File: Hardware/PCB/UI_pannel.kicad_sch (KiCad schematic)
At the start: 0 parts

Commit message: added UI
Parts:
- added C? (x4): C, symbol Device:C
- added J2: FH34SRJ-24S-0.5SH(50), symbol FPC_Connectors:FH34SRJ-24S-0.5SH(50)
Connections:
- new net +18V: C?.1, C?.1, J2.21
- new net +3.3V: C?.1, C?.1, J2.22, J2.23
- new net GND: C?.2, C?.2, C?.2, C?.2, J2.1, J2.11, J2.14, J2.17, J2.18, J2.2, J2.20, J2.24, J2.5, J2.8
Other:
- note added: "Connector for screen"
- note added: "Screen"
- note added: "pwm for constan current"

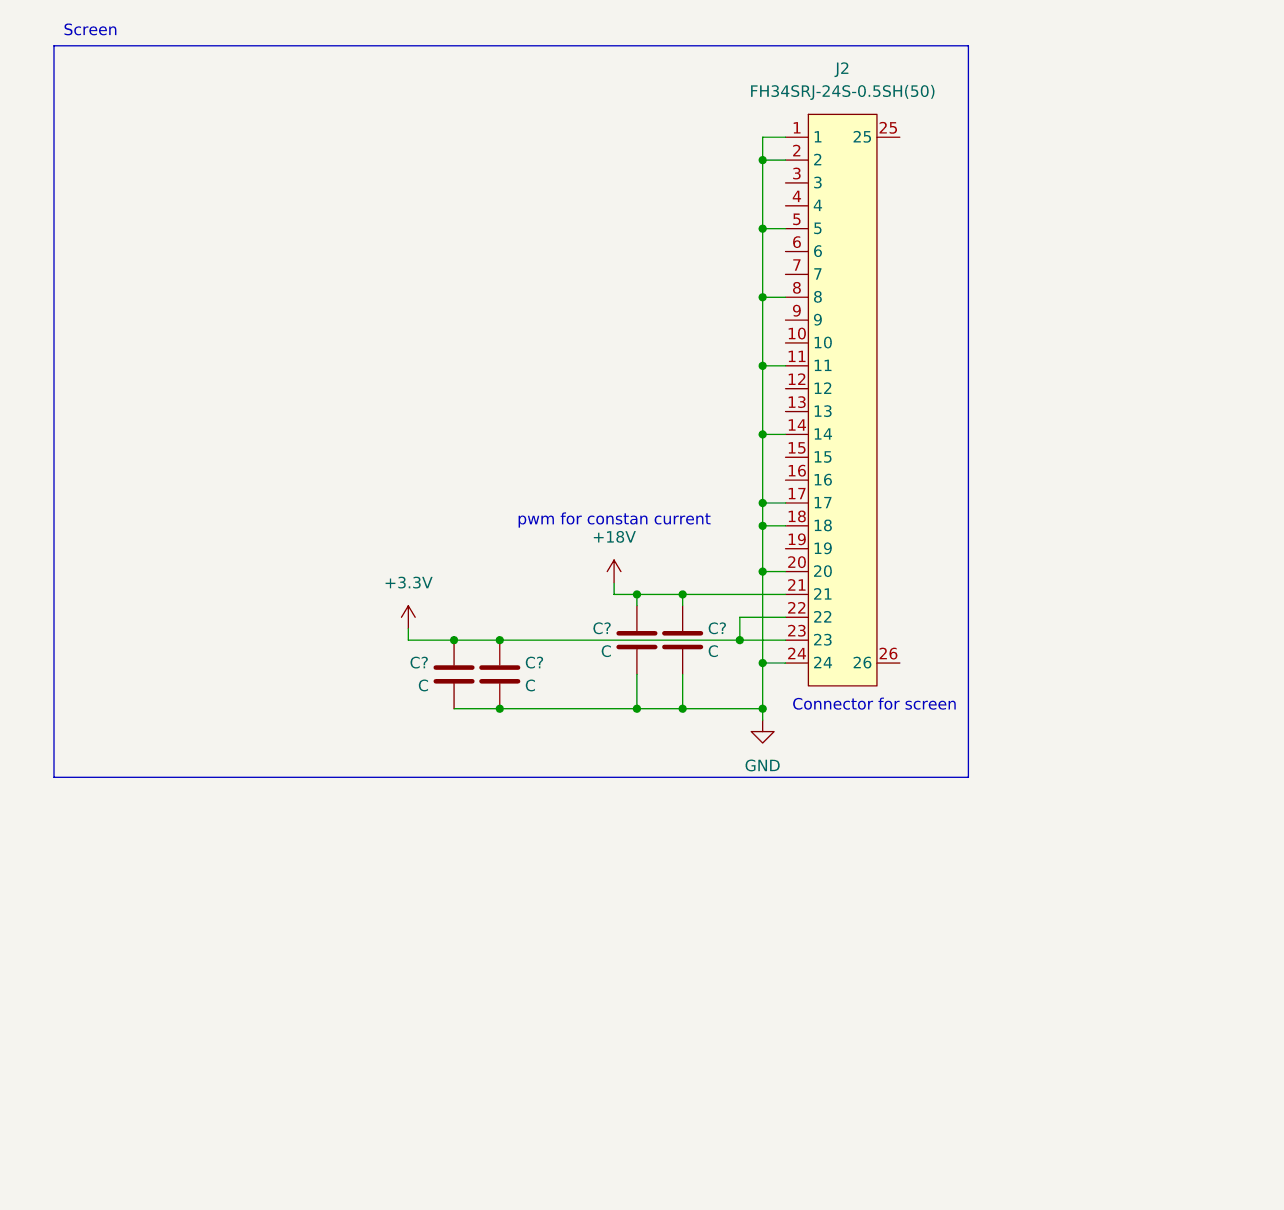
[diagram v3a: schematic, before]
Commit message: added buttons
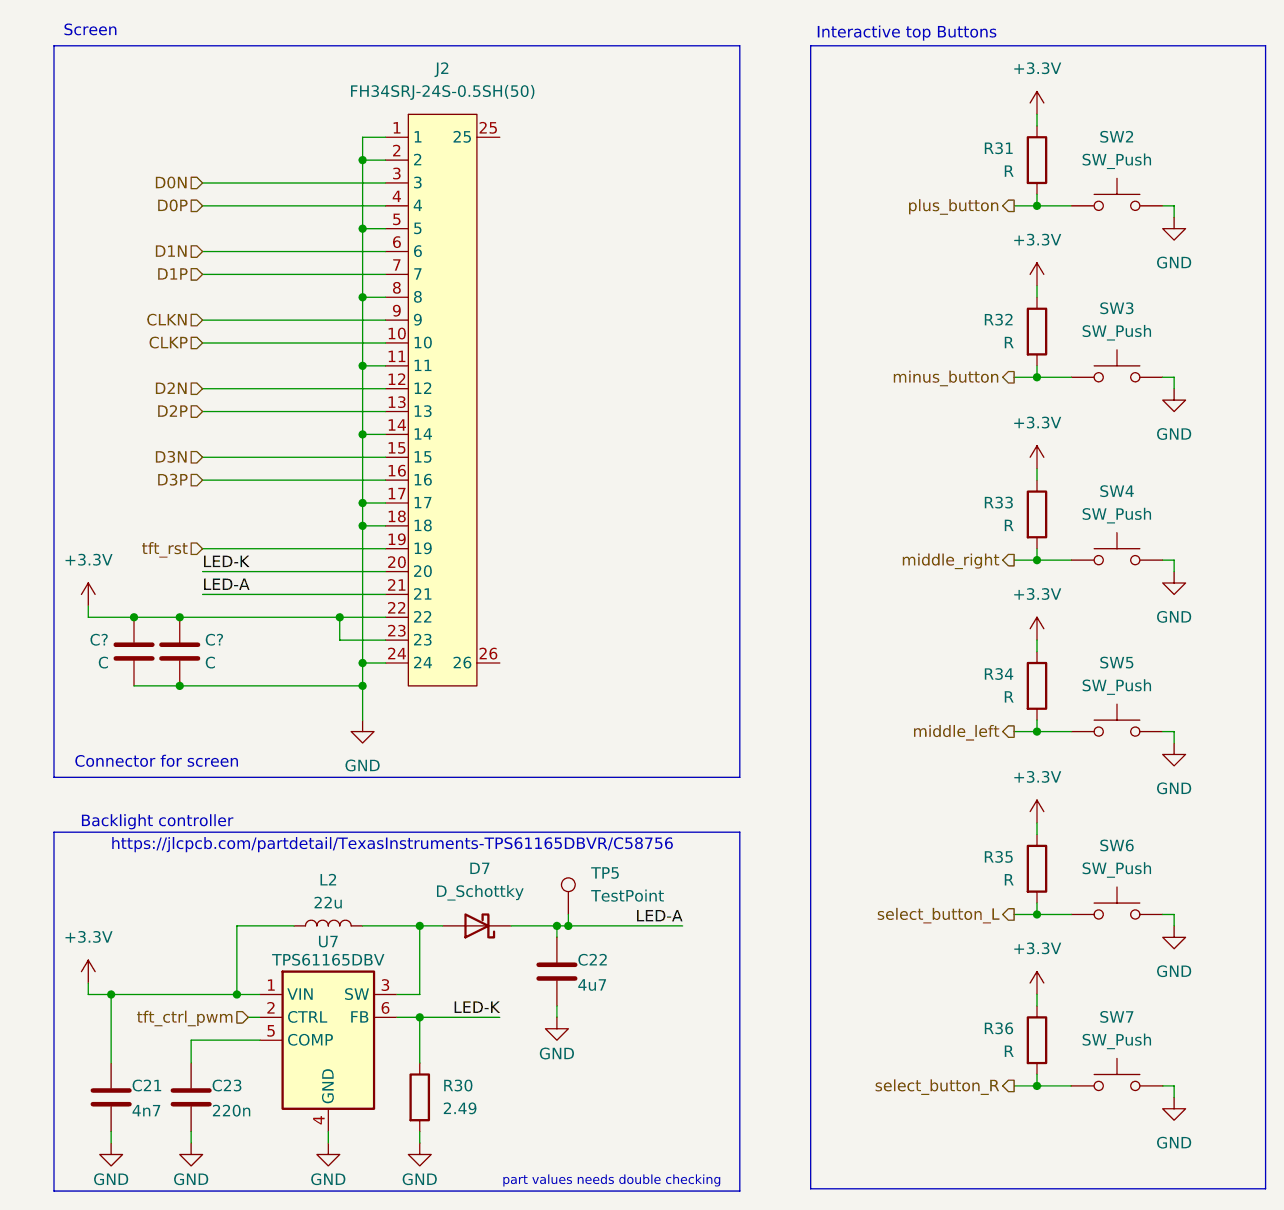
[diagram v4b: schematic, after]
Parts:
- removed C? (x2): C, symbol Device:C
- added C21: 4n7, symbol Device:C
- added C22: 4u7, symbol Device:C
- added C23: 220n, symbol Device:C
- added D7: D_Schottky, symbol Device:D_Schottky
- added L2: 22u, symbol Device:L
- added R30: 2.49, symbol Device:R
- added R31, R32, R33, R34, R35, R36: R, symbol Device:R
- added SW2, SW3, SW4, SW5, SW6, SW7: SW_Push, symbol Switch:SW_Push
- added TP5: TestPoint, symbol Connector:TestPoint
- added U7: TPS61165DBV, Package_TO_SOT_SMD:SOT-23-6, symbol Driver_LED:TPS61165DBV
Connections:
- net +3.3V: now also C21.1, L2.1, R31.1, R32.1, R33.1, R34.1, R35.1, R36.1, U7.1 (VIN)
- net GND: now also C21.2, C22.2, C23.2, R30.2, SW2.2, SW3.2, SW4.2, SW5.2, SW6.2, SW7.2, U7.4 (GND); no longer J2.20
- net CLKP: now reaches J2.10
- net D2N: now reaches J2.12
- net D2P: now reaches J2.13
- net D3N: now reaches J2.15
- net D3P: now reaches J2.16
- net tft_rst: now reaches J2.19
- net D0N: now reaches J2.3
- net D0P: now reaches J2.4
- net D1N: now reaches J2.6
- net D1P: now reaches J2.7
- net CLKN: now reaches J2.9
- net +18V renamed LED-A
- net LED-A: now also C22.1, D7.1 (K), TP5.1
- new net: C23.1, U7.5 (COMP)
- new net: D7.2 (A), L2.2, U7.3 (SW)
- new net LED-K: J2.20, R30.1, U7.6 (FB)
- new net middle_left: R34.2, SW5.1
- new net middle_right: R33.2, SW4.1
- new net minus_button: R32.2, SW3.1
- new net plus_button: R31.2, SW2.1
- new net select_button_L: R35.2, SW6.1
- new net select_button_R: R36.2, SW7.1
- new net tft_ctrl_pwm: U7.2 (CTRL)
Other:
- note added: "Backlight controller"
- note added: "Interactive top Buttons"
- note added: "https://jlcpcb.com/partdetail/TexasInstruments-TPS61165DBVR/C58756"
- note added: "part values needs double checking"
- note removed: "pwm for constan current"
- moved on the sheet: C?, J2

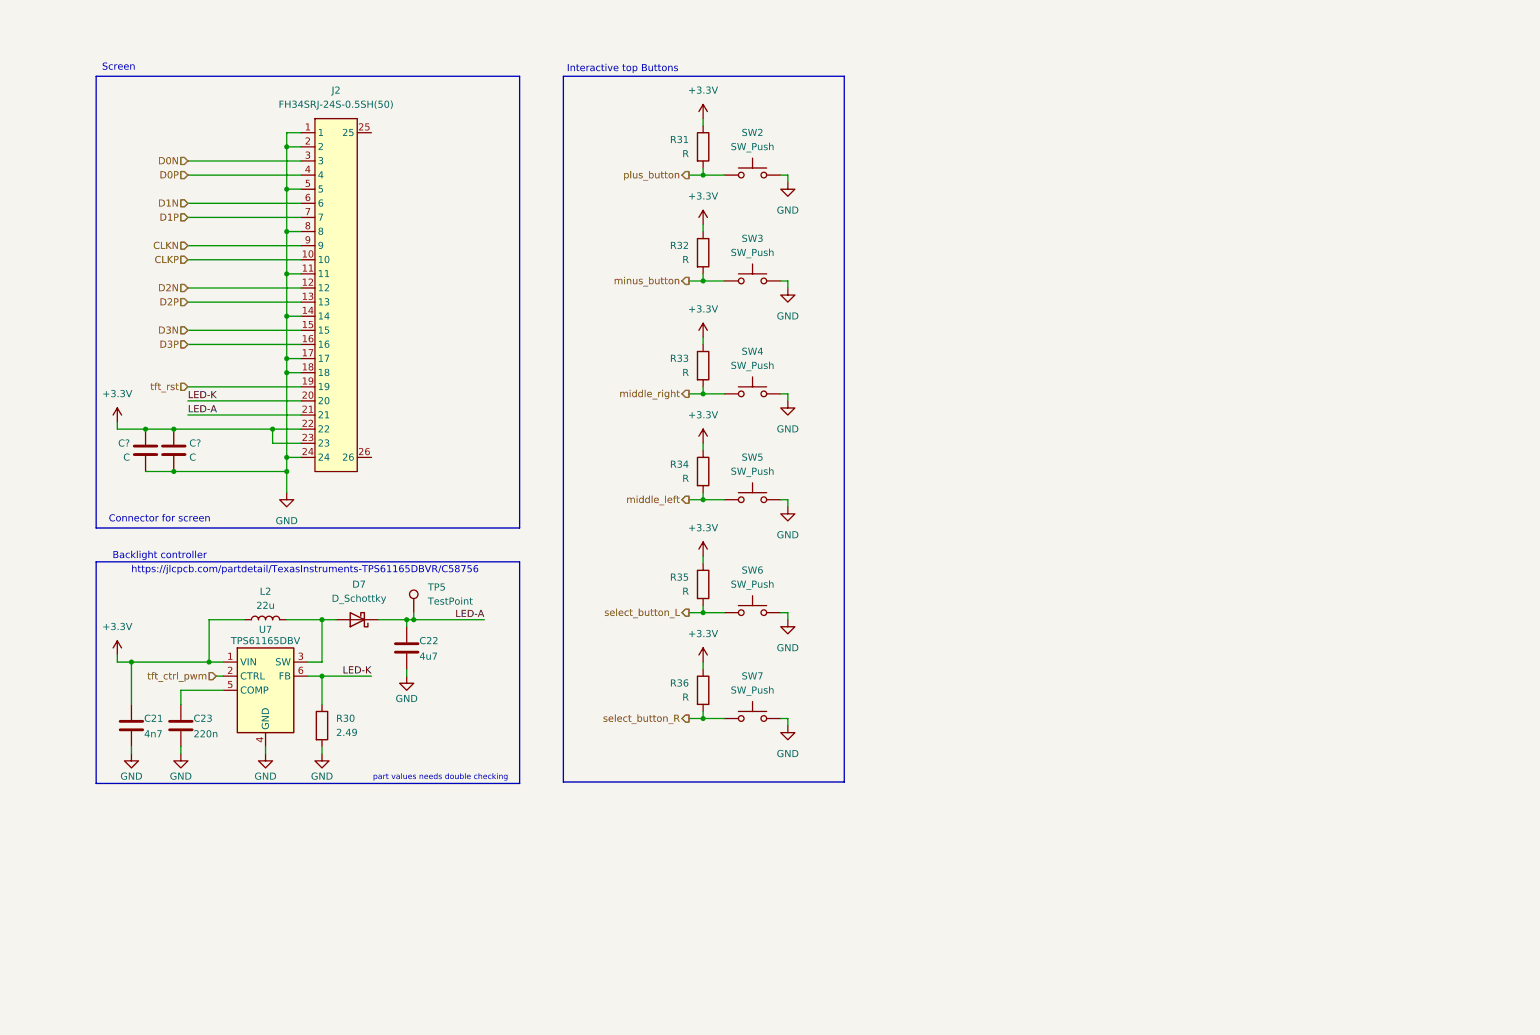
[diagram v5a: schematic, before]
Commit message: added new screen and updated mcu to a more compatible one
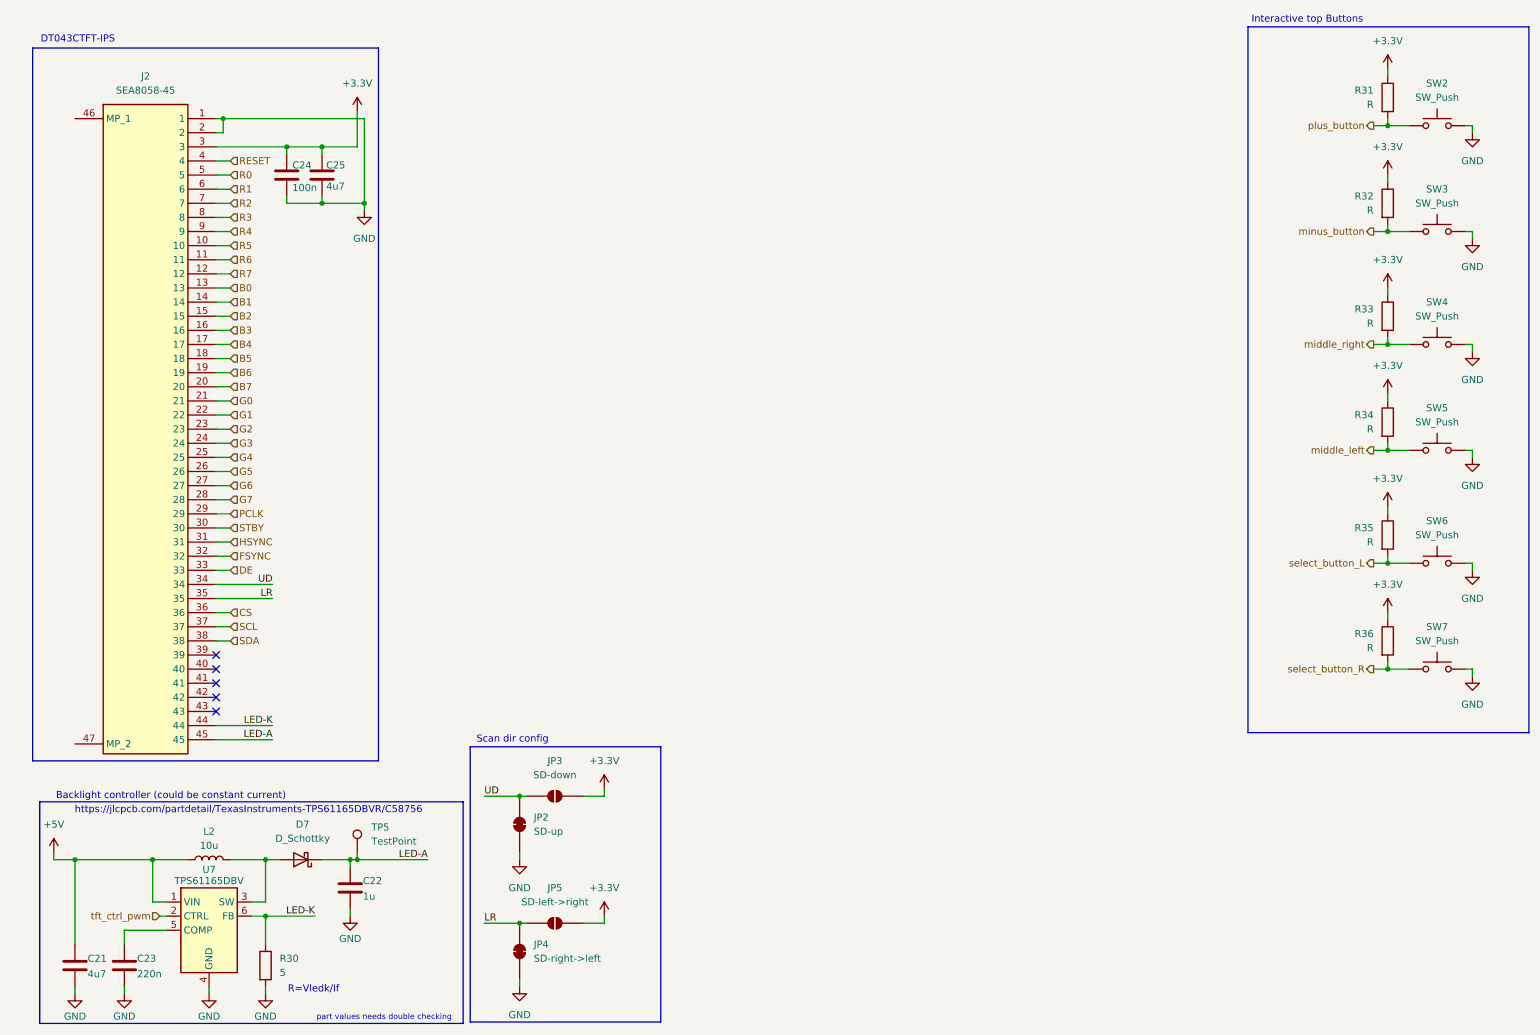
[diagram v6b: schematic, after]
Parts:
- removed C? (x2): C, symbol Device:C
- removed J2: FH34SRJ-24S-0.5SH(50), symbol FPC_Connectors:FH34SRJ-24S-0.5SH(50)
- added C24: 100n, symbol Device:C
- added C25: 4u7, symbol Device:C
- added J2: SEA8058-45, SEA805845, symbol custom_connectors:SEA8058-45
- added JP2: SD-up, symbol Jumper:SolderJumper_2_Bridged
- added JP3: SD-down, symbol Jumper:SolderJumper_2_Open
- added JP4: SD-right->left, symbol Jumper:SolderJumper_2_Bridged
- added JP5: SD-left->right, symbol Jumper:SolderJumper_2_Open
- C21: value 4n7 -> 4u7
- C22: value 4u7 -> 1u
- L2: value 22u -> 10u
- R30: value 2.49 -> 5
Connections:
- net +3.3V: now also C24.1, C25.1, J2.3, JP3.2 (B), JP5.2 (B); no longer C21.1, L2.1, U7.1 (VIN)
- net GND: now also C24.2, C25.2, J2.1, J2.2, JP2.1 (A), JP4.1 (A)
- net LED-A: now also J2.45
- net LED-K: now also J2.44
- new net +5V: C21.1, L2.1, U7.1 (VIN)
- new net B0: J2.13
- new net B1: J2.14
- new net B2: J2.15
- new net B3: J2.16
- new net B4: J2.17
- new net B5: J2.18
- new net B6: J2.19
- new net B7: J2.20
- new net CS: J2.36
- new net DE: J2.33
- new net FSYNC: J2.32
- new net G0: J2.21
- new net G1: J2.22
- new net G2: J2.23
- new net G3: J2.24
- new net G4: J2.25
- new net G5: J2.26
- new net G6: J2.27
- new net G7: J2.28
- new net HSYNC: J2.31
- new net LR: J2.35, JP4.2 (B), JP5.1 (A)
- new net PCLK: J2.29
- new net R0: J2.5
- new net R1: J2.6
- new net R2: J2.7
- new net R3: J2.8
- new net R4: J2.9
- new net R5: J2.10
- new net R6: J2.11
- new net R7: J2.12
- new net RESET: J2.4
- new net SCL: J2.37
- new net SDA: J2.38
- new net STBY: J2.30
- new net UD: J2.34, JP2.2 (B), JP3.1 (A)
- no-connect marks 0 -> 5
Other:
- note added: "Backlight controller (could be constant current)"
- note added: "DT043CTFT-IPS"
- note added: "R=Vledk/If"
- note added: "Scan dir config"
- note removed: "Backlight controller"
- note removed: "Connector for screen"
- note removed: "Screen"
- moved on the sheet: C21, C22, C23, D7, L2, R30, R31, R32, R33, R34, R35, R36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
